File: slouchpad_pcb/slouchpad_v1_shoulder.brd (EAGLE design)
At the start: 36.8 x 15.2 mm, 3 parts

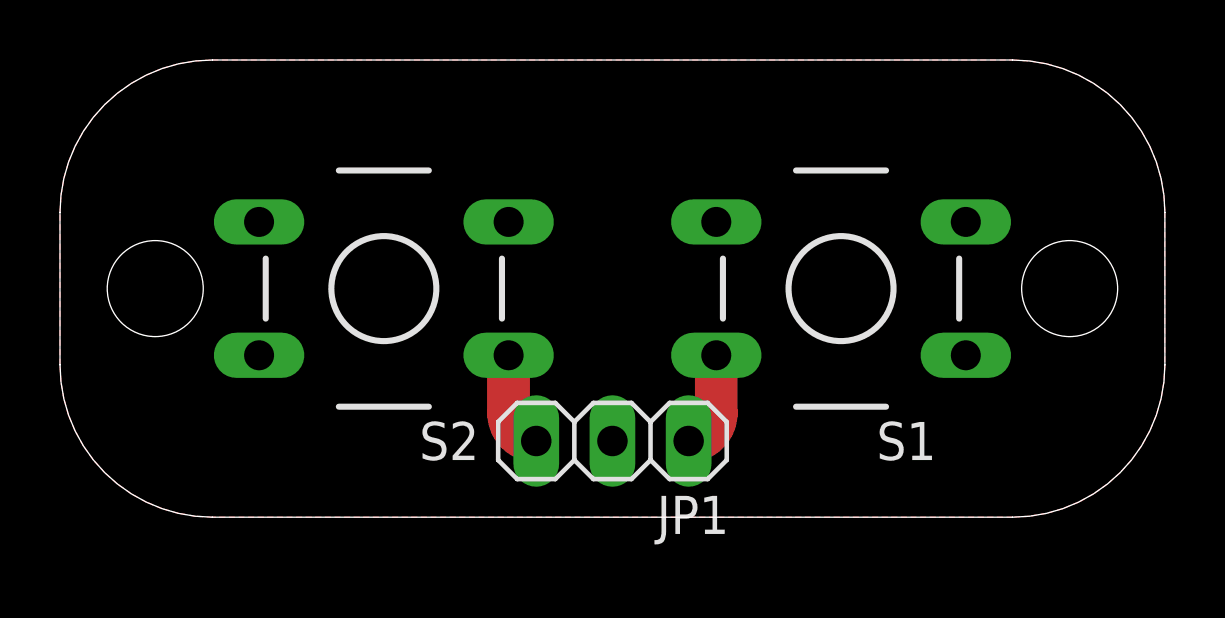
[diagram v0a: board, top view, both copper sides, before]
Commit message: Retooled the project to be a modular joypad
Rather than being a shield for the SparkFun Pro Micro Arduino, the slouchpad will simply be a modular joypad for use with any microcontroller.

Modified the license to reflect the removal of the SparkFun Pro Micro

Removed backup design files

Created button layout for left thumb pad

Modified all board positions to units of mm where possible.

Signed-off-by: Eric Jones <eric.r.k.jones@gmail.com>
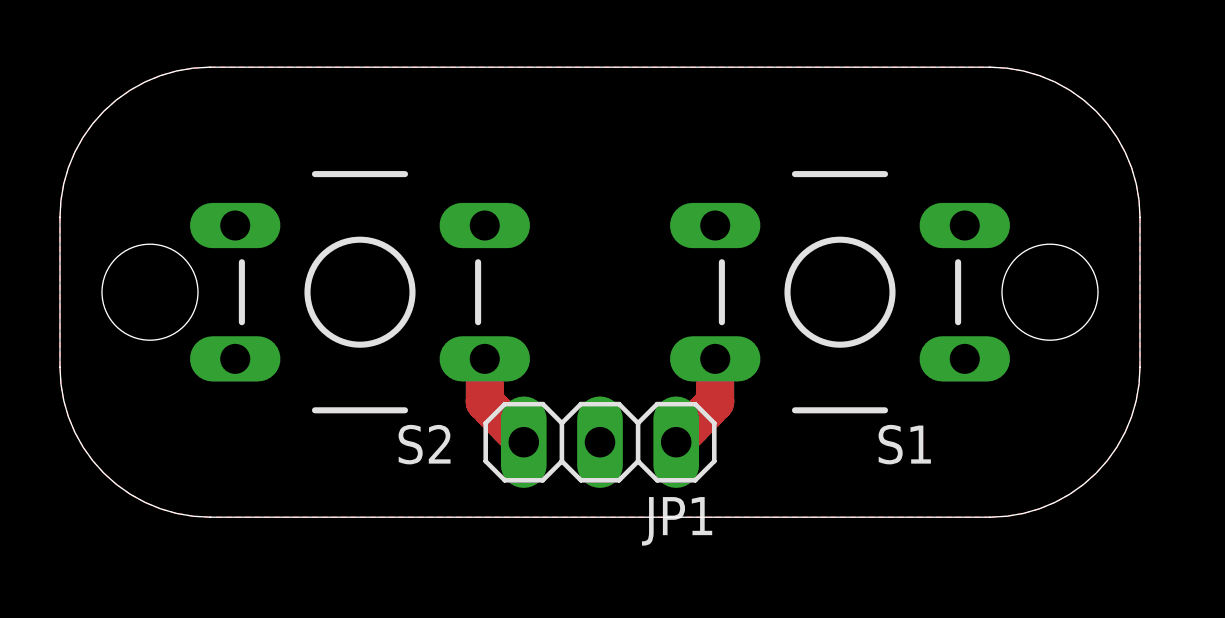
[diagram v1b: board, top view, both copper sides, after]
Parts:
- moved S2 0.80 mm to (10.0, 7.50)
- moved JP1 0.42 mm to (18.0, 2.50)
- moved S1 0.13 mm to (26.0, 7.50)
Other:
- board size 36.8 x 15.2 mm -> 36 x 15 mm
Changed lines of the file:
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@@
 <setting verticaltext="up"/>
 </settings>
-<grid distance="0.025" unitdist="inch" unit="inch" style="lines" multiple="1" display="yes" altdistance="0.025" altunitdist="inch" altunit="inch"/>
+<grid distance="1" unitdist="mm" unit="mm" style="lines" multiple="1" display="yes" altdistance="0.025" altunitdist="inch" altunit="inch"/>
 <layers>
 <layer number="1" name="Top" color="4" fill="1" visible="yes" active="yes"/>
@@
 <layer number="42" name="bRestrict" color="1" fill="10" visible="yes" active="yes"/>
 <layer number="43" name="vRestrict" color="2" fill="10" visible="yes" active="yes"/>
-<layer number="44" name="Drills" color="7" fill="1" visible="no" active="yes"/>
+<layer number="44" name="Drills" color="7" fill="1" visible="yes" active="yes"/>
 <layer number="45" name="Holes" color="7" fill="1" visible="yes" active="yes"/>
 <layer number="46" name="Milling" color="3" fill="1" visible="no" active="yes"/>
@@
 <board>
 <plain>
-<wire x1="0" y1="10.16" x2="0" y2="5.08" width="0" layer="20"/>
-<wire x1="0" y1="5.08" x2="5.08" y2="0" width="0" layer="20" curve="90"/>
-<wire x1="5.08" y1="0" x2="31.75" y2="0" width="0" layer="20"/>
-<wire x1="31.75" y1="0" x2="36.83" y2="5.08" width="0" layer="20" curve="90"/>
-<wire x1="36.83" y1="5.08" x2="36.83" y2="10.16" width="0" layer="20"/>
-<wire x1="36.83" y1="10.16" x2="31.75" y2="15.24" width="0" layer="20" curve="90"/>
-<wire x1="31.75" y1="15.24" x2="5.08" y2="15.24" width="0" layer="20"/>
-<wire x1="5.08" y1="15.24" x2="0" y2="10.16" width="0" layer="20" curve="90"/>
-<hole x="3.175" y="7.62" drill="3.2"/>
-<hole x="33.655" y="7.62" drill="3.2"/>
+<wire x1="0" y1="10" x2="0" y2="5" width="0" layer="20"/>
+<wire x1="0" y1="5" x2="5" y2="0" width="0" layer="20" curve="90"/>
+<wire x1="5" y1="0" x2="31" y2="0" width="0" layer="20"/>
+<wire x1="31" y1="0" x2="36" y2="5" width="0" layer="20" curve="90"/>
+<wire x1="36" y1="5" x2="36" y2="10" width="0" layer="20"/>
+<wire x1="36" y1="10" x2="31" y2="15" width="0" layer="20" curve="90"/>
+<wire x1="31" y1="15" x2="5" y2="15" width="0" layer="20"/>
+<wire x1="5" y1="15" x2="0" y2="10" width="0" layer="20" curve="90"/>
+<hole x="3" y="7.5" drill="3.2"/>
+<hole x="33" y="7.5" drill="3.2"/>
 </plain>
 <attributes>
@@
 </autorouter>
 <elements>
-<element name="JP1" library="pinhead" package="1X03" value="" x="18.415" y="2.54" rot="R180"/>
-<element name="S1" library="switch-tact" package="DTS-8" value="DTS-8" x="26.035" y="7.62" rot="R180"/>
-<element name="S2" library="switch-tact" package="DTS-8" value="DTS-8" x="10.795" y="7.62" rot="R180"/>
+<element name="JP1" library="pinhead" package="1X03" value="" x="18" y="2.5" rot="R180"/>
+<element name="S1" library="switch-tact" package="DTS-8" value="DTS-8" x="26" y="7.5" rot="R180"/>
+<element name="S2" library="switch-tact" package="DTS-8" value="DTS-8" x="10" y="7.5" rot="R180"/>
 </elements>
 <signals>
@@
 <contactref element="S1" pad="2"/>
 <contactref element="JP1" pad="1"/>
-<wire x1="21.87575" y1="3.46075" x2="21.87575" y2="5.3975" width="1.4224" layer="1"/>
-<wire x1="21.87575" y1="3.46075" x2="20.955" y2="2.54" width="1.4224" layer="1" curve="-90"/>
-<wire x1="21.87575" y1="5.3975" x2="30.19425" y2="5.3975" width="0" layer="19" extent="1-1"/>
+<wire x1="20.54" y1="2.5" x2="21.84075" y2="3.84075" width="1.27" layer="1"/>
+<wire x1="21.84075" y1="3.84075" x2="21.84075" y2="5.2775" width="1.27" layer="1"/>
+<wire x1="21.84075" y1="5.2775" x2="30.15925" y2="5.2775" width="0" layer="19" extent="1-1"/>
 </signal>
 <signal name="S2" airwireshidden="yes">
@@
 <contactref element="S2" pad="2"/>
 <contactref element="JP1" pad="3"/>
-<wire x1="14.95425" y1="5.3975" x2="14.95425" y2="3.46075" width="1.4224" layer="1"/>
-<wire x1="14.95425" y1="3.46075" x2="15.875" y2="2.54" width="1.4224" layer="1" curve="90"/>
-<wire x1="6.63575" y1="5.3975" x2="14.95425" y2="5.3975" width="0" layer="19" extent="1-1"/>
+<wire x1="15.46" y1="2.5" x2="14.15925" y2="3.84075" width="1.27" layer="1"/>
+<wire x1="14.15925" y1="3.84075" x2="14.15925" y2="5.2775" width="1.27" layer="1"/>
+<wire x1="5.84075" y1="5.2775" x2="14.15925" y2="5.2775" width="0" layer="19" extent="1-1"/>
 </signal>
 <signal name="GND">
@@
 <contactref element="JP1" pad="2"/>
 <polygon width="1.27" layer="1" thermals="no">
-<vertex x="5.08" y="15.24"/>
-<vertex x="31.75" y="15.24" curve="-90"/>
-<vertex x="36.83" y="10.16"/>
-<vertex x="36.83" y="5.08" curve="-90"/>
-<vertex x="31.75" y="0"/>
-<vertex x="5.08" y="0" curve="-90"/>
-<vertex x="0" y="5.08"/>
-<vertex x="0" y="10.16" curve="-90"/>
+<vertex x="31" y="0"/>
+<vertex x="5" y="0" curve="-90"/>
+<vertex x="0" y="5"/>
+<vertex x="0" y="10" curve="-90"/>
+<vertex x="5" y="15"/>
+<vertex x="31" y="15" curve="-90"/>
+<vertex x="36" y="10"/>
+<vertex x="36" y="5" curve="-90"/>
 </polygon>
 </signal>

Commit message: Finished silkscreen of boards
Moved traces to bottom layer to represent design intention
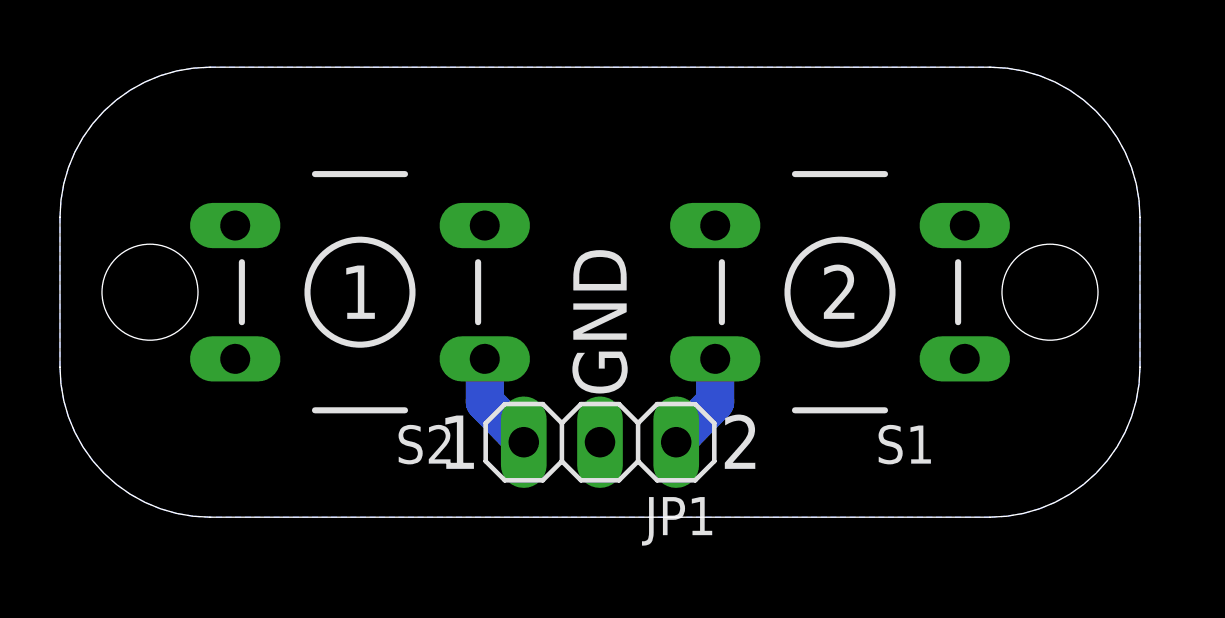
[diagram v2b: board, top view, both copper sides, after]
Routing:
- added copper zone on layer 16, net GND
- removed copper zone on layer 1, net GND
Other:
- board text added: "1"
- board text added: "2"
- board text added: "GND"
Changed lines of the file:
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@@
 <setting verticaltext="up"/>
 </settings>
-<grid distance="1" unitdist="mm" unit="mm" style="lines" multiple="1" display="yes" altdistance="0.025" altunitdist="inch" altunit="inch"/>
+<grid distance="0.5" unitdist="mm" unit="mm" style="lines" multiple="1" display="yes" altdistance="0.025" altunitdist="inch" altunit="inch"/>
 <layers>
 <layer number="1" name="Top" color="4" fill="1" visible="yes" active="yes"/>
@@
 <layer number="20" name="Dimension" color="15" fill="1" visible="yes" active="yes"/>
 <layer number="21" name="tPlace" color="7" fill="1" visible="yes" active="yes"/>
-<layer number="22" name="bPlace" color="7" fill="1" visible="yes" active="yes"/>
-<layer number="23" name="tOrigins" color="15" fill="1" visible="yes" active="yes"/>
-<layer number="24" name="bOrigins" color="15" fill="1" visible="yes" active="yes"/>
-<layer number="25" name="tNames" color="7" fill="1" visible="yes" active="yes"/>
-<layer number="26" name="bNames" color="7" fill="1" visible="yes" active="yes"/>
-<layer number="27" name="tValues" color="7" fill="1" visible="yes" active="yes"/>
-<layer number="28" name="bValues" color="7" fill="1" visible="yes" active="yes"/>
+<layer number="22" name="bPlace" color="7" fill="1" visible="no" active="yes"/>
+<layer number="23" name="tOrigins" color="15" fill="1" visible="no" active="yes"/>
+<layer number="24" name="bOrigins" color="15" fill="1" visible="no" active="yes"/>
+<layer number="25" name="tNames" color="7" fill="1" visible="no" active="yes"/>
+<layer number="26" name="bNames" color="7" fill="1" visible="no" active="yes"/>
+<layer number="27" name="tValues" color="7" fill="1" visible="no" active="yes"/>
+<layer number="28" name="bValues" color="7" fill="1" visible="no" active="yes"/>
 <layer number="29" name="tStop" color="7" fill="3" visible="no" active="yes"/>
 <layer number="30" name="bStop" color="7" fill="6" visible="no" active="yes"/>
@@
 <layer number="97" name="Info" color="7" fill="1" visible="no" active="no"/>
 <layer number="98" name="Guide" color="6" fill="1" visible="no" active="no"/>
+<layer number="100" name="tSilk" color="15" fill="1" visible="yes" active="yes"/>
 </layers>
 <board>
@@
 <hole x="3" y="7.5" drill="3.2"/>
 <hole x="33" y="7.5" drill="3.2"/>
+<text x="10" y="7.5" size="1.778" layer="100" align="center">1</text>
+<text x="26" y="7.5" size="1.778" layer="100" align="center">2</text>
+<text x="18" y="4" size="1.778" layer="100" rot="R90" align="center-left">GND</text>
+<text x="14" y="2.5" size="1.778" layer="100" rot="R180" align="center-left">1</text>
+<text x="22" y="2.5" size="1.778" layer="100" align="center-left">2</text>
 </plain>
 <attributes>
@@
 <contactref element="S1" pad="2"/>
 <contactref element="JP1" pad="1"/>
-<wire x1="20.54" y1="2.5" x2="21.84075" y2="3.84075" width="1.27" layer="1"/>
-<wire x1="21.84075" y1="3.84075" x2="21.84075" y2="5.2775" width="1.27" layer="1"/>
+<wire x1="20.54" y1="2.5" x2="21.84075" y2="3.84075" width="1.27" layer="16"/>
+<wire x1="21.84075" y1="3.84075" x2="21.84075" y2="5.2775" width="1.27" layer="16"/>
 <wire x1="21.84075" y1="5.2775" x2="30.15925" y2="5.2775" width="0" layer="19" extent="1-1"/>
 </signal>
@@
 <contactref element="S2" pad="2"/>
 <contactref element="JP1" pad="3"/>
-<wire x1="15.46" y1="2.5" x2="14.15925" y2="3.84075" width="1.27" layer="1"/>
-<wire x1="14.15925" y1="3.84075" x2="14.15925" y2="5.2775" width="1.27" layer="1"/>
+<wire x1="15.46" y1="2.5" x2="14.15925" y2="3.84075" width="1.27" layer="16"/>
+<wire x1="14.15925" y1="3.84075" x2="14.15925" y2="5.2775" width="1.27" layer="16"/>
 <wire x1="5.84075" y1="5.2775" x2="14.15925" y2="5.2775" width="0" layer="19" extent="1-1"/>
 </signal>
@@
 <contactref element="S1" pad="4"/>
 <contactref element="JP1" pad="2"/>
-<polygon width="1.27" layer="1" thermals="no">
+<polygon width="1.27" layer="16" thermals="no">
 <vertex x="31" y="0"/>
 <vertex x="5" y="0" curve="-90"/>
